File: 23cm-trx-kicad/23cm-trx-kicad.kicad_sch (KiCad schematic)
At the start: 23 parts, among them SW1 RotaryEncoder_Switch, U1 LCD 20x4, U2 L78L09_SOT89

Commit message: More schematic
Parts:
- added C10: C_Small, symbol Device:C_Small
- added C11: 1uF, symbol Device:C_Small
- added C9: 100nF, symbol Device:C_Small
- added D2, D3: 1N4148, Diode_THT:D_DO-35_SOD27_P7.62mm_Horizontal, symbol Diode:1N4148
- added MK1: Microphone, symbol Device:Microphone
- added R11: 15K, symbol Device:R_Small_US
- added R12, R13: 100K, symbol Device:R_Small_US
- added R14, R15: 150K, symbol Device:R_Small_US
- added U3: LM741, symbol Amplifier_Operational:LM741
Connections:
- net GND: now also D2.2 (A), D3.1 (K), MK1.2 (+), R12.2, R15.2, U3.4 (V-)
- net MCU-AUDIO: now also C11.1, U3.3 (+)
- new net: C9.1, D2.1 (K), D3.2 (A), R12.1, R13.2
- new net: C9.2, R11.1, U3.6
- new net: R14.2, R15.1
- new net: R11.2, U3.2 (-)
- new net: C11.2, MK1.1 (-)
- new net +TX: C10.1, R14.1, U3.7 (V+)
- new net 100nF: C10.2
- new net MIC-AUDIO: R13.1
- no-connect marks 4 -> 6
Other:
- note added: ">3.5A"
- note added: "MICROPHONE AUDIO"
- note added: "ORIGINAL DESIGN USED 13.8V SUPPLY WHICH ARE STANDARD IN HAM CIRCLES ECHOING ANCIENT LEAD ACID BATTERY CHARGES. THESE DAYS 24V SUPPLIES ARE WAY MORE AVAILABLE AND CHEAPER SO WE LOOK TO SUPPORT THESE."
- note removed: "I=?"
- note removed: "ORIGINAL DESIGN USED 13.8V SUPPLY WHICH IS STANDARD IN HAM CIRCLES OWING TO ANCIENT LEAD ACID BATTERY CHARGES. THESE DAYS 24V SUPPLIES ARE WAY MORE AVAILABLE AND CHEAPER SO WE ADD LOOK TO SUPPORT THESE."
- moved on the sheet: A1, C1, C2, C3, C4, C5, C6, C7, C8, D1, R1, R10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

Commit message: Further schematic work
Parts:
- removed R12: 100K, symbol Device:R_Small_US
- removed R9: 25K, symbol Device:R_Small_US
- added C12: 220nF, symbol Device:C_Polarized_Small
- added RV1, RV4: 100K, symbol Device:R_Potentiometer
- added RV2: 25K, symbol Device:R_Potentiometer_Trim
- added RV3: 50K, symbol Device:R_Potentiometer_Trim
- added U4: LM386, symbol Amplifier_Audio:LM386
- C10: value C_Small -> 100nF
- R1: value 50K -> 10
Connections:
- net 100nF is gone; now on net GND: C10.2
- net 13.8V: now also R1.1
- net 5V: now also RV3.2; no longer R1.1, U1.2 (VDD), U1.3 (VO)
- net GND: now also C12.2, RV1.3, RV2.3, RV3.3, RV4.1, U4.2 (-), U4.4 (GND); no longer R1.2
- net MCU-AUDIO: now also R14.2, R15.1
- net at C9.1, D2.1 (K), D3.2 (A): now also RV4.3; no longer R13.2
- net at C7.1, R8.2: now also RV2.1; no longer C8.2
- new net: C8.2, RV2.2
- new net: RV1.2, U4.3 (+)
- new net: C12.1, R1.2, U4.6 (V+)
- new net: RV3.1, U1.2 (VDD), U1.3 (VO)
- new net: R13.2, RV4.2
- new net AUDIO-OUT: RV1.1
- no-connect marks 6 -> 9
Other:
- note added: "MCU-ORIGINATED AUDIO"
- note added: "ORIGINAL DESIGN USED PB6/PB7 (NOT EXPOSED ON THE ARDUINO NANO V3) SO WE USE THESE ANALOG ONLY PINS: WILL REQUIRE CODE TWEAK."
- note added: "SPEAKER"
- note removed: "MCU-ORIGINATED AUDIO PROCESSING"
- note removed: "ORIGINAL DESIGN USED PB6/PB7 (APPARENTLY NOT EXPORTED FROM ATMEGA328P ON ARDUINO NANO) SO WE USE THESE ANALOG-ONLY PINS. WILL REQUIRE CODE TWEAK."
- moved on the sheet: A1, C1, C10, C11, C2, C3, C4, C5, C6, C7, C8, C9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

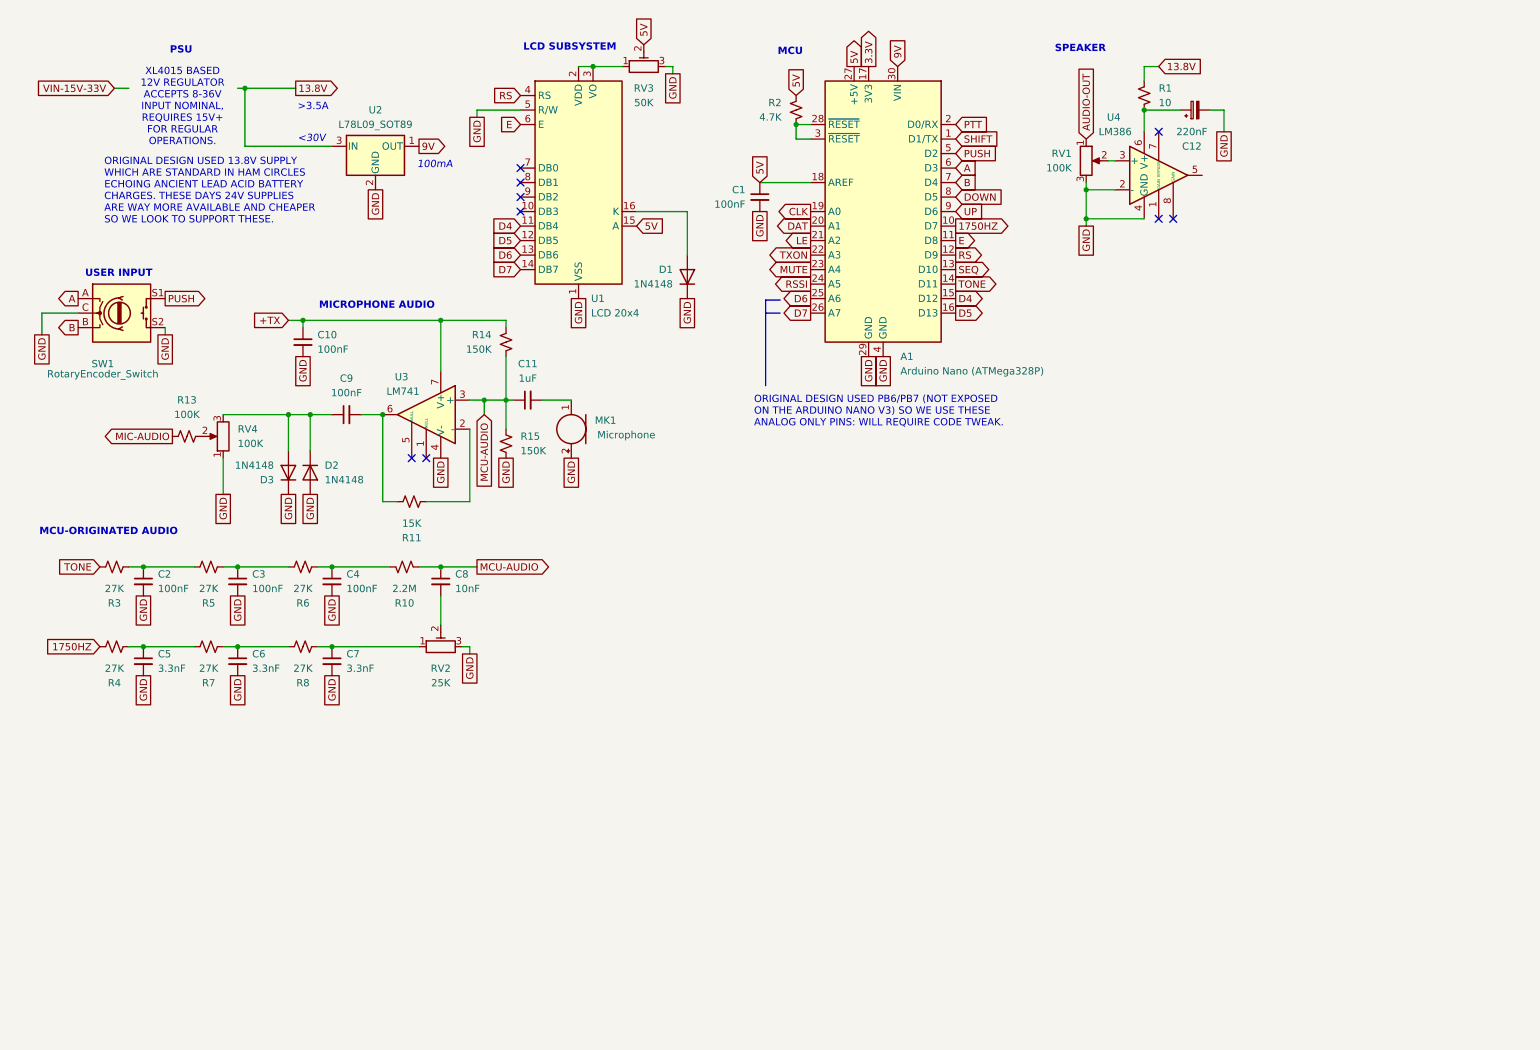
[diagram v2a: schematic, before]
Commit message: LCD to I2C
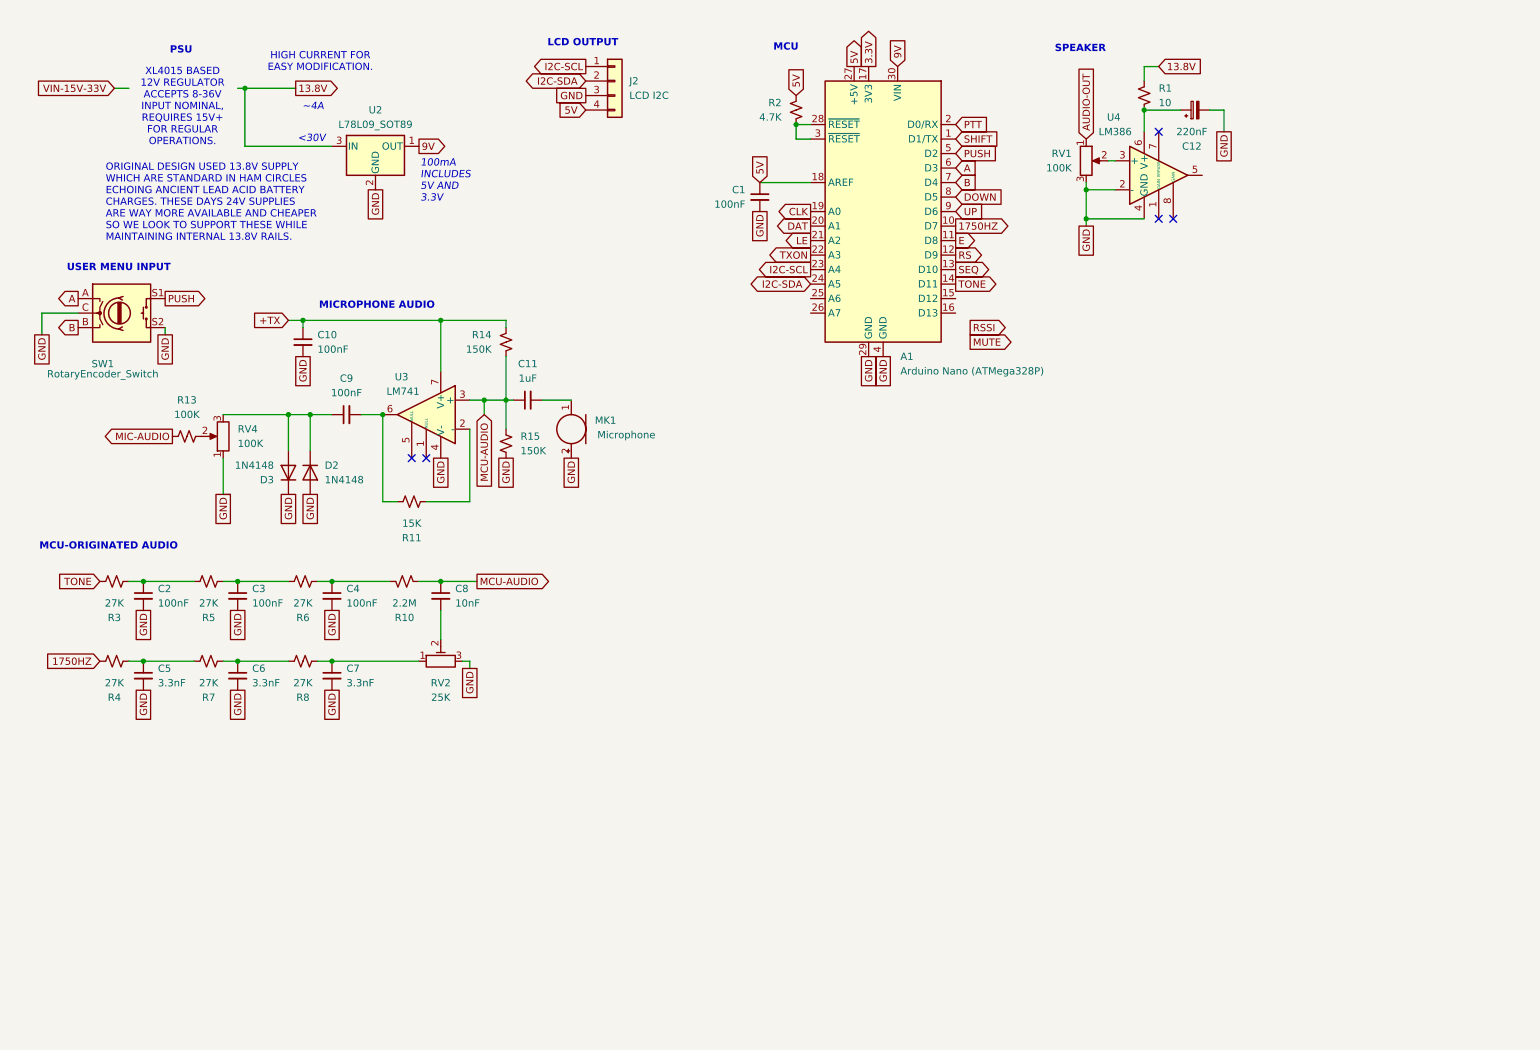
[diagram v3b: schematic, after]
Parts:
- removed D1: 1N4148, Diode_THT:D_DO-35_SOD27_P7.62mm_Horizontal, symbol Diode:1N4148
- removed RV3: 50K, symbol Device:R_Potentiometer_Trim
- removed U1: LCD 20x4, Display:NHD-0420H1Z, symbol Display_Character:NHD-0420H1Z
- added J2: LCD I2C, symbol Connector_Generic:Conn_01x04
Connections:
- net 5V: now also J2.4 (Pin_4)
- net GND: now also J2.3 (Pin_3)
- net MUTE: no longer A1.23 (A4)
- net RSSI: no longer A1.24 (A5)
- net D4: no longer names the net of A1.15 (D12)
- net D5: no longer names the net of A1.16 (D13)
- net D6: no longer names the net of A1.25 (A6)
- net D7: no longer names the net of A1.26 (A7)
- new net I2C-SCL: A1.23 (A4), J2.1 (Pin_1)
- new net I2C-SDA: A1.24 (A5), J2.2 (Pin_2)
- no-connect marks 9 -> 5
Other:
- note added: "100mA INCLUDES 5V AND 3.3V"
- note added: "HIGH CURRENT FOR EASY MODIFICATION."
- note added: "LCD OUTPUT"
- note added: "ORIGINAL DESIGN USED 13.8V SUPPLY WHICH ARE STANDARD IN HAM CIRCLES ECHOING ANCIENT LEAD ACID BATTERY CHARGES. THESE DAYS 24V SUPPLIES ARE WAY MORE AVAILABLE AND CHEAPER SO WE LOOK TO SUPPORT THESE WHILE MAINTAINING INTERNAL 13.8V RAILS."
- note added: "USER MENU INPUT"
- note added: "~4A"
- note removed: "100mA"
- note removed: ">3.5A"
- note removed: "LCD SUBSYSTEM"
- note removed: "ORIGINAL DESIGN USED 13.8V SUPPLY WHICH ARE STANDARD IN HAM CIRCLES ECHOING ANCIENT LEAD ACID BATTERY CHARGES. THESE DAYS 24V SUPPLIES ARE WAY MORE AVAILABLE AND CHEAPER SO WE LOOK TO SUPPORT THESE."
- note removed: "ORIGINAL DESIGN USED PB6/PB7 (NOT EXPOSED ON THE ARDUINO NANO V3) SO WE USE THESE ANALOG ONLY PINS: WILL REQUIRE CODE TWEAK."
- note removed: "USER INPUT"
- moved on the sheet: C2, C3, C4, C5, C6, C7, C8, R10, R3, R4, R5, R6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

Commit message: Further schematic work
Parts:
- added C13: 220uF, symbol Device:C_Polarized_Small
- added C14: 47nF, symbol Device:C_Small
- added LS1: Speaker, symbol Device:Speaker
- added R9: 12, symbol Device:R_Small_US
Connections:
- net GND: now also C14.2, LS1.2
- net at U4.5: now also C13.1, R9.1
- new net: C13.2, LS1.1
- new net: C14.1, R9.2
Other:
- note added: "MICROPHONE AUDIO AMPLIFIER"
- note added: "PHASE LOCK LOOP"
- note removed: "MICROPHONE AUDIO"
- moved on the sheet: A1, C1, C10, C11, C12, C2, C3, C4, C5, C6, C7, C8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

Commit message: Further schematic work
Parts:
- added J1: LCD BACKLIGHT, symbol Connector_Generic:Conn_01x02
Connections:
- net 5V: now also J2.2 (Pin_2); no longer J2.4 (Pin_4)
- net GND: now also J2.1 (Pin_1), J1.2 (Pin_2); no longer J2.3 (Pin_3)
- net I2C-SCL: now also A1.24 (A5), J2.4 (Pin_4); no longer A1.23 (A4), J2.1 (Pin_1)
- net I2C-SDA: now also A1.23 (A4), J2.3 (Pin_3); no longer A1.24 (A5), J2.2 (Pin_2)
- new net LCD-BACKLIGHT: J1.1 (Pin_1)
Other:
- note added: "APPROX. 4A"
- note added: "MICROPHONE AUDIO PRE-AMPLIFIER"
- note added: "ORIGINAL DESIGN USED 13.8V SUPPLY WHICH IS APPARENTLY THE STANDARD IN HAM CIRCLES, ECHOING ANCIENT LEAD ACID BATTERY CHARGES. THESE DAYS 24V SUPPLIES ARE WAY MORE AVAILABLE AND CHEAPER SO WE LOOK TO SUPPORT THESE WHILE MAINTAINING INTERNAL 13.8V RAILS."
- note added: "POWER AMPLIFIER (PA)"
- note added: "POWER AMPLIFIER AND SPEAKER"
- note added: "POWER SUPPLY UNIT (PSU)"
- note removed: "MICROPHONE AUDIO AMPLIFIER"
- note removed: "ORIGINAL DESIGN USED 13.8V SUPPLY WHICH ARE STANDARD IN HAM CIRCLES ECHOING ANCIENT LEAD ACID BATTERY CHARGES. THESE DAYS 24V SUPPLIES ARE WAY MORE AVAILABLE AND CHEAPER SO WE LOOK TO SUPPORT THESE WHILE MAINTAINING INTERNAL 13.8V RAILS."
- note removed: "PSU"
- note removed: "SPEAKER"
- note removed: "~4A"
- moved on the sheet: A1, C1, C10, C11, C12, C13, C14, C2, C3, C4, C5, C6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

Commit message: Further schematic work
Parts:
- added Q1: BC547, Package_TO_SOT_THT:TO-92_Inline, symbol Transistor_BJT:BC547
- added Q2: BD138, Package_TO_SOT_THT:TO-126-3_Vertical, symbol Transistor_BJT:BD138
- added Q3: BC557, Package_TO_SOT_THT:TO-92_Inline, symbol Transistor_BJT:BC557
- added R12, R19: 4.7K, symbol Device:R_Small_US
- added R16: 470, symbol Device:R_Small_US
- added R17, R18: 15K, symbol Device:R_Small_US
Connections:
- net +TX: now also Q2.2 (C), R19.2
- net GND: now also Q1.3 (E)
- net TXON: now also R12.1
- new net: Q3.2 (B), R18.1, R19.1
- new net: Q2.1 (E), Q3.3 (E), R17.1, R18.2
- new net: Q1.1 (C), R12.2
- new net: Q2.3 (B), R16.1, R17.2
- new net: Q1.2 (B), R16.2
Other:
- note added: "DRAW SYMBOL FOR ADF4153"
- note added: "DRAW SYMBOL FOR TCXO-13MHZ"
- note added: "NOTE PIN NUMBERS ARE MISMATCHED TO ORIGINAL PDF SCHEMATIC. ASSUME KICAD SYMBOL BUG, SINCE RESOLVED."

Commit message: Further schematic work
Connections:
- net TONE renamed CTCSS-TONE
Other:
- note added: "APPARENTLY "OLD EUROPE" REPEATER ACCESS TONE."
- note added: "AUDIO INPUT OCCURS HERE"
- note added: "AUDIO OUTPUT OCCURS HERE"
- note added: "NORMAL REPEATER ACCESS SYSTEM."
- note added: "POWER INPUT OCCURS HERE"
- note added: "THIS SECTION IS USED TO FACILITATE MCU-BASED TONE GENERATION FOR GRANTING REPEATER ACCESS. IT CAN BE OMITTED FOR MAKING DIRECT COMMUNICATIONS."
- note added: "USER INTERFACE INPUT OCCURS HERE"
- note added: "USER INTERFACE OUTPUT OCCURS HERE"
- moved on the sheet: C2, C3, C4, C5, C6, C7, C8, J1, J2, R10, R3, R4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

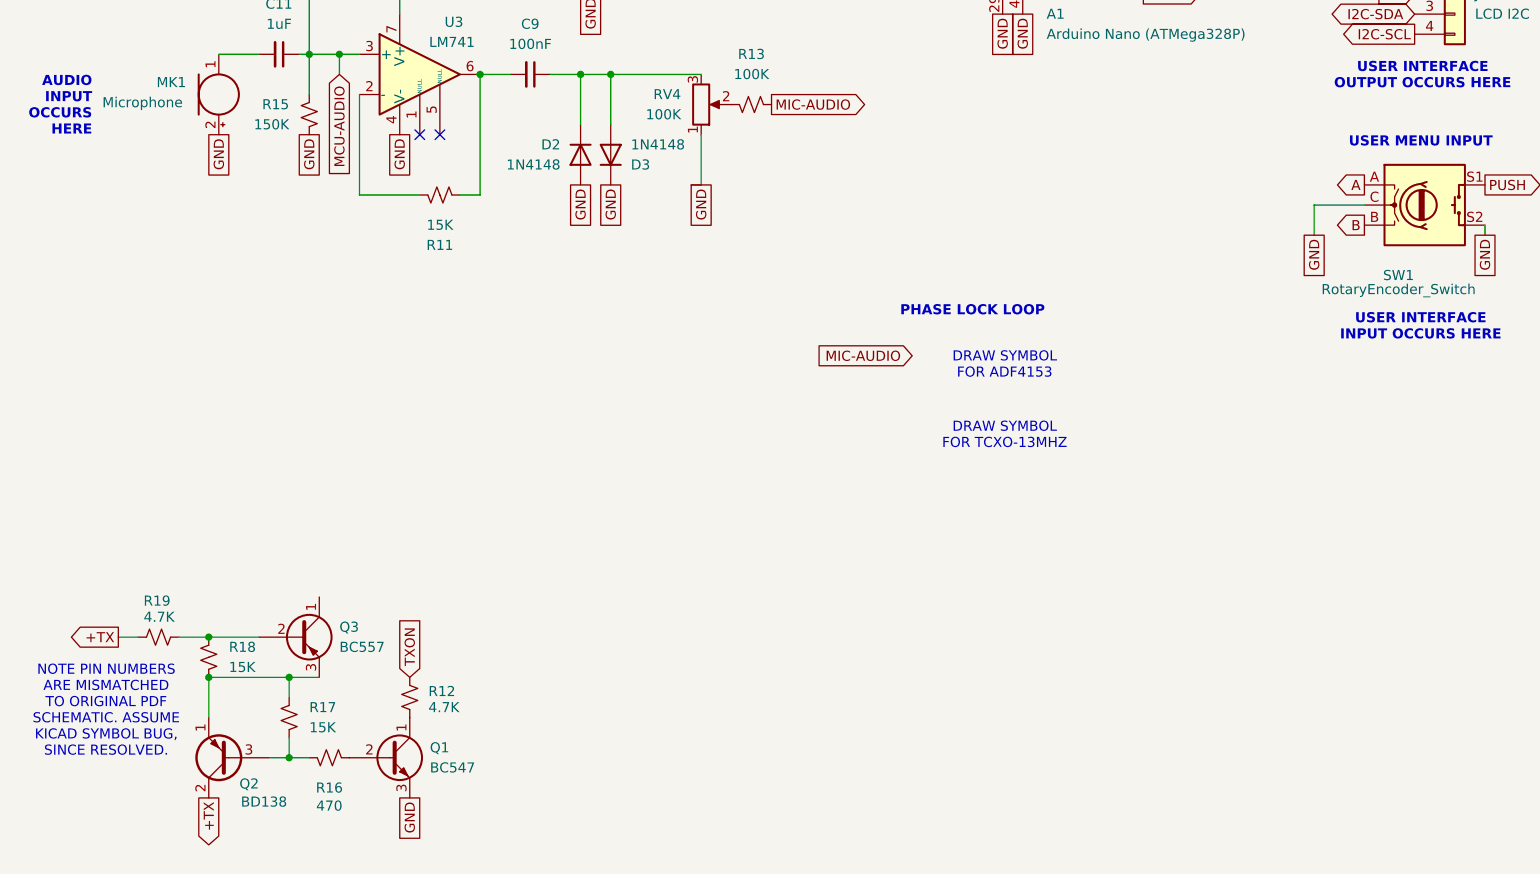
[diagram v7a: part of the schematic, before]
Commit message: More schematic work; additional project symbol table
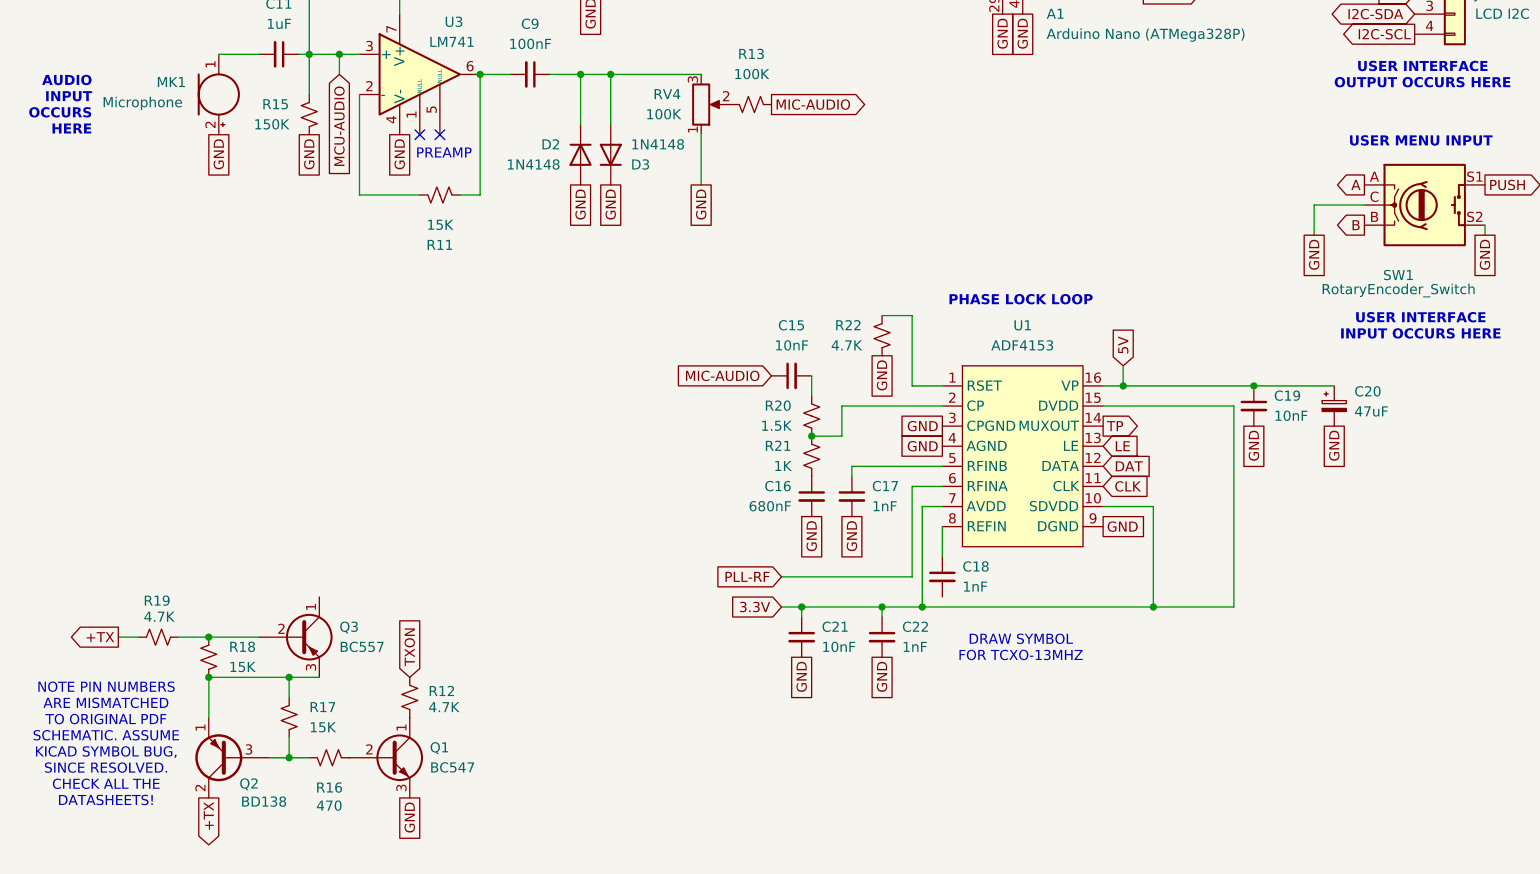
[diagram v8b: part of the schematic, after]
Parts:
- added C15, C19, C21: 10nF, symbol Device:C_Small
- added C16: 680nF, symbol Device:C_Small
- added C17, C18, C22: 1nF, symbol Device:C_Small
- added C20: 47uF, symbol Device:C_Polarized_Small
- added R20: 1.5K, symbol Device:R_Small_US
- added R21: 1K, symbol Device:R_Small_US
- added R22: 4.7K, symbol Device:R_Small_US
- added U1: ADF4153, Package_SO:HTSSOP-16-1EP_4.4x5mm_P0.65mm_EP3.4x5mm_Mask3x3mm_ThermalVias, symbol 23cm-trx-kicad-symbol-library:ADF4153
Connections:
- net 3.3V: now also C21.1, C22.1, U1.10 (SDVDD), U1.15 (DVDD), U1.7 (AVDD)
- net 5V: now also C19.1, C20.1, U1.16 (VP)
- net CLK: now also U1.11 (CLK)
- net DAT: now also U1.12 (DATA)
- net GND: now also C16.2, C17.2, C19.2, C20.2, C21.2, C22.2, R22.2, U1.3 (CPGND), U1.4 (AGND), U1.9 (DGND)
- net LE: now also U1.13 (LE)
- net MIC-AUDIO: now also C15.1
- new net: C15.2, R20.1
- new net: C17.1, U1.5 (RFINB)
- new net: R20.2, R21.1, U1.2 (CP)
- new net: C16.1, R21.2
- new net: C18.1, U1.8 (REFIN)
- new net: R22.1, U1.1 (RSET)
- new net PLL-RF: U1.6 (RFINA)
- new net TP: U1.14 (MUXOUT)
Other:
- note added: "NOTE PIN NUMBERS ARE MISMATCHED TO ORIGINAL PDF SCHEMATIC. ASSUME KICAD SYMBOL BUG, SINCE RESOLVED. CHECK ALL THE DATASHEETS!"
- note added: "PREAMP"
- note removed: "DRAW SYMBOL FOR ADF4153"
- note removed: "NOTE PIN NUMBERS ARE MISMATCHED TO ORIGINAL PDF SCHEMATIC. ASSUME KICAD SYMBOL BUG, SINCE RESOLVED."
